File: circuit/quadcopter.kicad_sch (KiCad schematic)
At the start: 119 parts, among them J1 Conn_01x01_Female, J10 Conn_01x01_Female, J13 Conn_01x01_Female, J15 Conn_01x01_Female, J16 Conn_01x01_Female, J17 Conn_01x01_Female, J18 USB_C_Receptacle_USB2.0, J19 Conn_01x08_Male, J2 Conn_01x01_Female, J21 Conn_01x01_Female, J22 Conn_01x01_Female, J23 Conn_01x01_Female, J24 Conn_01x01_Female, J25 Conn_01x01_Female, J26 Conn_01x01_Female, J28 Conn_01x01_Female, J29 Conn_01x01_Female, J3 Conn_01x01_Female, J30 Conn_01x01_Female, J31 Conn_01x01_Female, J32 Conn_01x01_Female, J33 Conn_01x01_Female, J34 Conn_01x01_Female, J37 Conn_01x01_Female, J4 Conn_01x01_Female, J40 Conn_01x01_Female, J41 Conn_01x01_Female, J42 Conn_01x01_Female, J43 Conn_01x01_Female, J44 Conn_01x01_Female, J45 Conn_01x01_Female, J46 Conn_01x01_Female, J47 Conn_01x01_Female, J48 Conn_01x01_Female, J49 Conn_01x01_Female, J5 Conn_Coaxial, J50 Conn_01x01_Female, J6 Conn_01x06_Male, J7 Conn_01x01_Female, J8 Conn_01x01_Female, J9 Conn_01x01_Female, Q1 AO3400A, SW1 SW_DIP_x01, U1 STM32G431CBU6, U2 ICM-42605, U3 DPS310, U4 3V3, U5 EUP3458 1.2A, 30V max input, 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, U6 2450FM07D0034T, U7 W25Q80DVUXIE TR (16M), U8 SX1281, U9 5v, 500mA, Y1 16M, Y2 52Mhz, 12pF

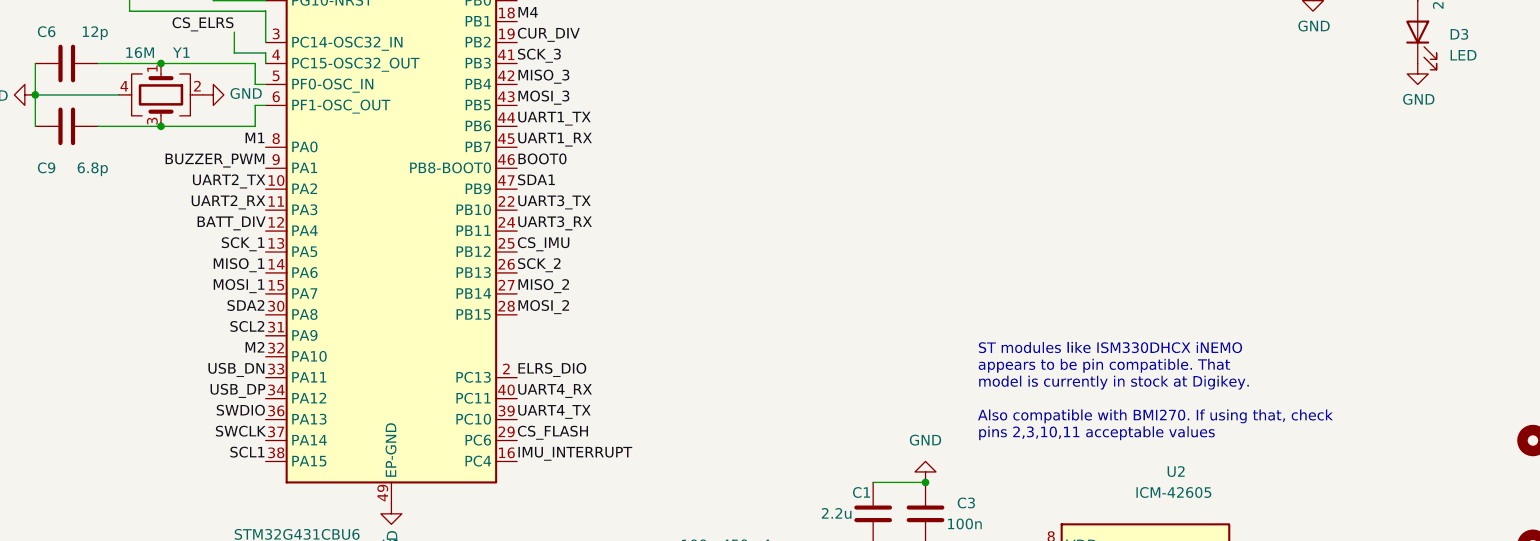
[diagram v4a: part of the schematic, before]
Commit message: A number of improvements to DSHOT/burst DMA logic
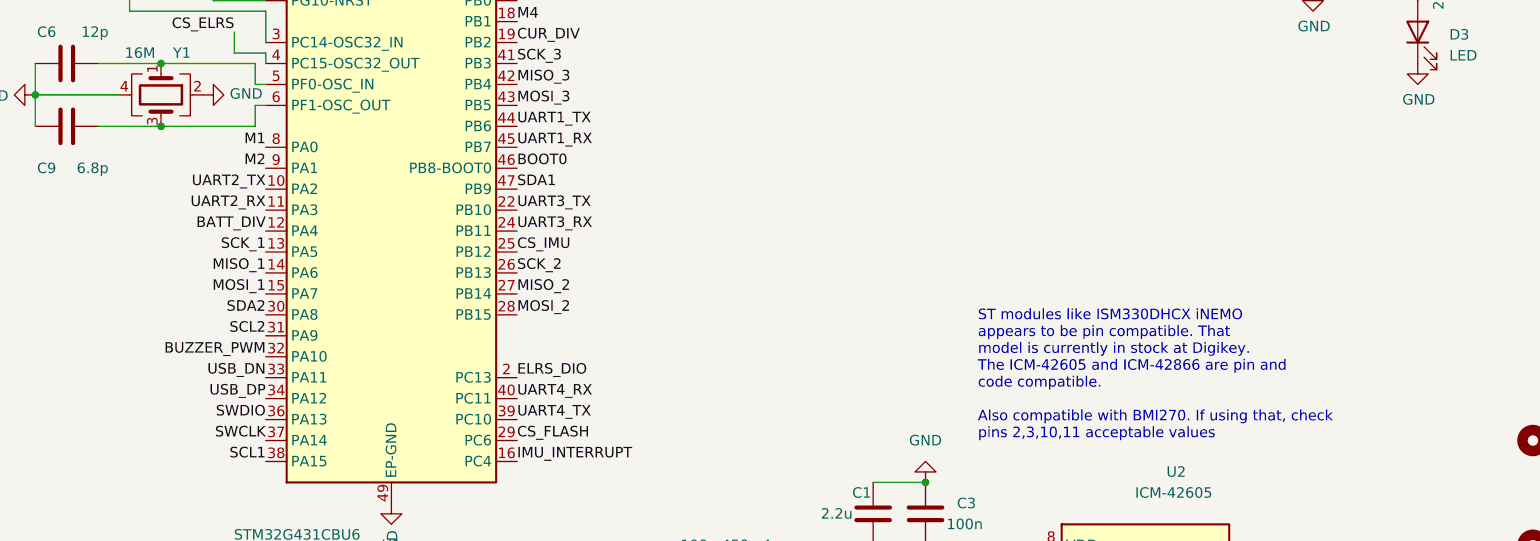
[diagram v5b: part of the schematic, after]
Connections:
- net BUZZER_PWM: now also U1.32 (PA10); no longer U1.9 (PA1)
- net M2: now also U1.9 (PA1); no longer U1.32 (PA10)
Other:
- note added: "ST modules like ISM330DHCX iNEMO appears to be pin compatible. That model is currently in stock at Digikey. The ICM-42605 and ICM-42866 are pin and code compatible. Also compatible with BMI270. If using that, check pins 2,3,10,11 acceptable values"
- note removed: "ST modules like ISM330DHCX iNEMO appears to be pin compatible. That model is currently in stock at Digikey. Also compatible with BMI270. If using that, check pins 2,3,10,11 acceptable values"
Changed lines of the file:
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@@
     (effects (font (size 1.27 1.27)) (justify left bottom))
   )
-  (text "ST modules like ISM330DHCX iNEMO\nappears to be pin compatible. That\nmodel is currently in stock at Digikey.\n\nAlso compatible with BMI270. If using that, check\npins 2,3,10,11 acceptable values\n"
+  (text "ST modules like ISM330DHCX iNEMO\nappears to be pin compatible. That\nmodel is currently in stock at Digikey.\nThe ICM-42605 and ICM-42866 are pin and\ncode compatible.\n\nAlso compatible with BMI270. If using that, check\npins 2,3,10,11 acceptable values\n"
     (at 199.39 114.3 0)
     (effects (font (size 1.27 1.27)) (justify left bottom))
@@
     (effects (font (size 1.27 1.27)) (justify left bottom))
   )
-  (label "M2" (at 113.03 104.14 180)
+  (label "M2" (at 113.03 81.28 180)
     (effects (font (size 1.27 1.27)) (justify right bottom))
   )
@@
     (effects (font (size 1.27 1.27)) (justify left bottom))
   )
-  (label "BUZZER_PWM" (at 113.03 81.28 180)
+  (label "BUZZER_PWM" (at 113.03 104.14 180)
     (effects (font (size 1.27 1.27)) (justify right bottom))
   )

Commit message: More work getting it towards a compilable state
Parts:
- J19: LCSC (none) -> C160407
- J6: LCSC (none) -> C160405; now left out of the parts list
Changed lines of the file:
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@@
+      (effects (font (size 1.27 1.27)) hide)
+    )
+    (property "LCSC" "C160407" (id 4) (at 478.79 53.34 0)
       (effects (font (size 1.27 1.27)) hide)
     )
@@
   )
   (symbol (lib_id "Connector:Conn_01x06_Male") (at 496.57 107.95 180) (unit 1)
-    (in_bom yes) (on_board yes)
+    (in_bom no) (on_board yes)
     (property "Reference" "J6" (id 0) (at 490.22 92.71 0)
       (effects (font (size 1.27 1.27)) (justify right))
@@
       (effects (font (size 1.27 1.27)) hide)
     )
+    (property "LCSC" "C160405" (id 4) (at 496.57 107.95 0)
+      (effects (font (size 1.27 1.27)) hide)
+    )

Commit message: Work on PIDs
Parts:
- U1: value STM32G431CBU6 -> STM32G474CEU6
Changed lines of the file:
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@@
     (in_bom yes) (on_board yes)
     (property "Reference" "U1" (id 0) (at 128.27 127 0))
-    (property "Value" "STM32G431CBU6" (id 1) (at 116.84 125.73 0))
+    (property "Value" "STM32G474CEU6" (id 1) (at 116.84 125.73 0))
     (property "Footprint" "Package_DFN_QFN:QFN-48-1EP_7x7mm_P0.5mm_EP5.6x5.6mm" (id 2) (at 115.57 119.38 0)
       (effects (font (size 1.27 1.27)) (justify right) hide)
@@
     )
     (path "/0340b3a8-59fc-4ac7-90dd-935a6d19ff49"
-      (reference "U1") (unit 1) (value "STM32G431CBU6") (footprint "Package_DFN_QFN:QFN-48-1EP_7x7mm_P0.5mm_EP5.6x5.6mm")
+      (reference "U1") (unit 1) (value "STM32G474CEU6") (footprint "Package_DFN_QFN:QFN-48-1EP_7x7mm_P0.5mm_EP5.6x5.6mm")
     )
     (path "/2606c3c7-aa7a-4631-9635-e40074c6e1f1"

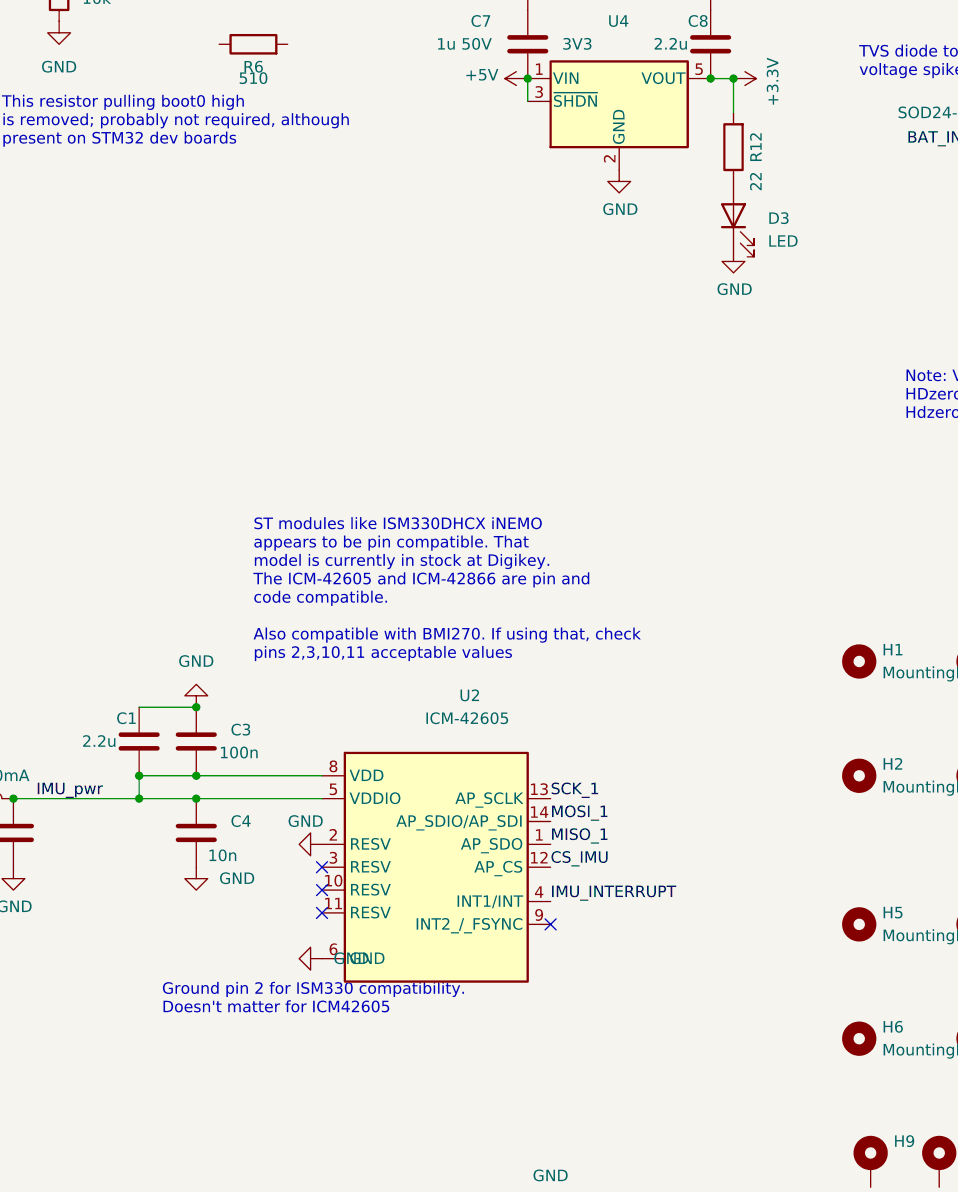
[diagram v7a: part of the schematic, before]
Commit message: More work on DSHOT, and fixes from testing on hardware
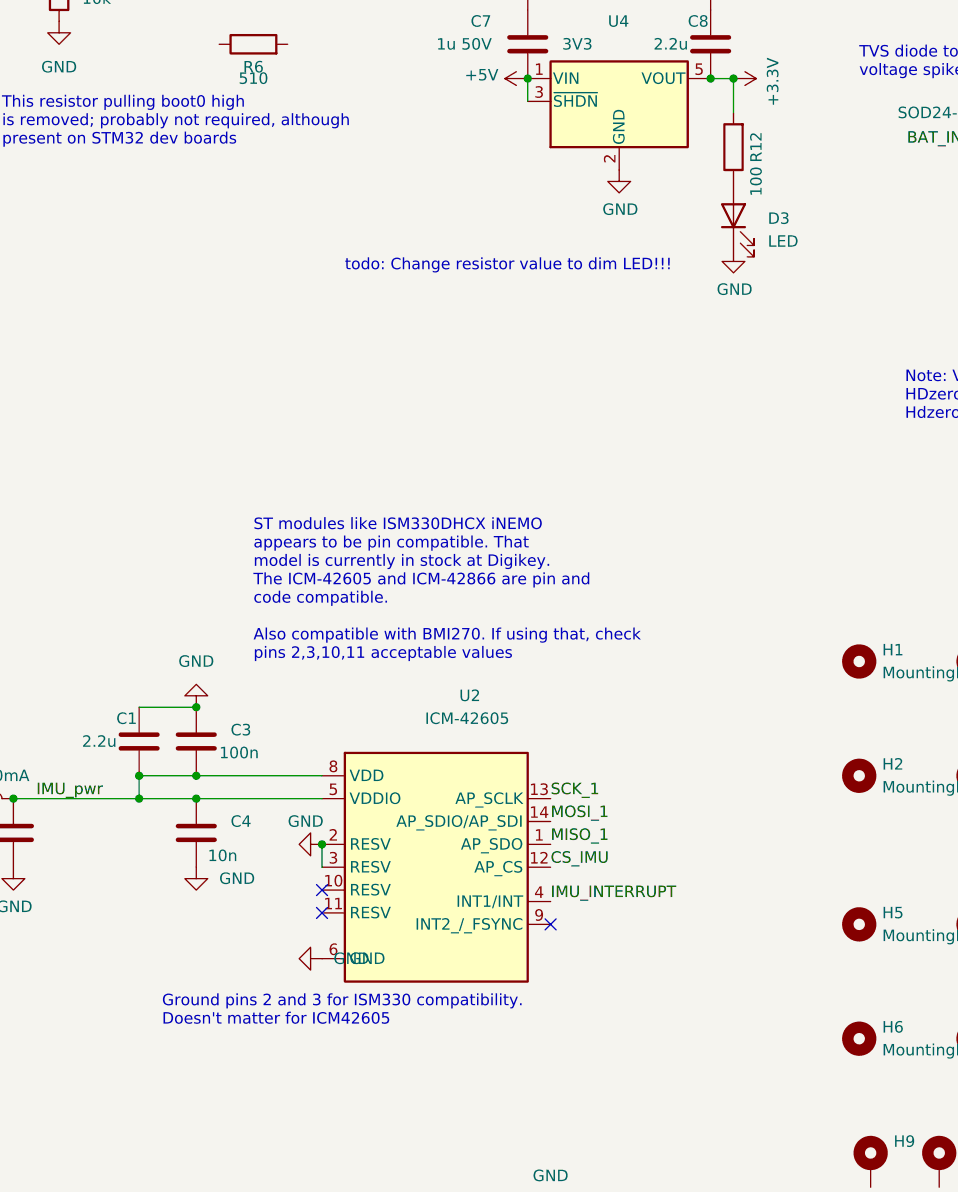
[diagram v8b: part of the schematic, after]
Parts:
- R12: value 22 -> 100; LCSC C25092 -> C25076
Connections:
- net GND: now also U2.3 (RESV)
- no-connect marks 9 -> 8
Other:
- note added: "Ground pins 2 and 3 for ISM330 compatibility. Doesn't matter for ICM42605"
- note added: "todo: Change resistor value to dim LED!!!"
- note removed: "Ground pin 2 for ISM330 compatibility. Doesn't matter for ICM42605"
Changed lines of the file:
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@@
   (junction (at 64.77 325.12) (diameter 0) (color 0 0 0 0)
   )
+  (junction (at 207.01 134.62) (diameter 0) (color 0 0 0 0)
+  )
   (junction (at 124.46 48.26) (diameter 0) (color 0 0 0 0)
   )
@@
   (no_connect (at 48.26 306.07))
   (no_connect (at 27.94 231.14))
-  (no_connect (at 207.01 137.16))
   (no_connect (at 207.01 139.7))
   (no_connect (at 207.01 142.24))
@@
     (stroke (width 0) (type default) (color 0 0 0 0))
   )
+  (wire (pts (xy 207.01 134.62) (xy 207.01 137.16))
+    (stroke (width 0) (type default) (color 0 0 0 0))
+  )
   (wire (pts (xy 289.56 -20.32) (xy 297.18 -20.32))
     (stroke (width 0) (type default) (color 0 0 0 0))
@@
     (effects (font (size 1.27 1.27)) (justify left bottom))
   )
-  (text "Ground pin 2 for ISM330 compatibility.\nDoesn't matter for ICM42605\n"
-    (at 189.23 153.67 0)
+  (text "todo: Change resistor value to dim LED!!!" (at 209.55 71.12 0)
+    (effects (font (size 1.27 1.27)) (justify left bottom))
+  )
+  (text "Ground pins 2 and 3 for ISM330 compatibility.\nDoesn't matter for ICM42605\n"
+    (at 189.23 154.94 0)
     (effects (font (size 1.27 1.27)) (justify left bottom))
   )
@@
     (in_bom yes) (on_board yes)
     (property "Reference" "R12" (id 0) (at 255.27 57.15 90))
-    (property "Value" "22" (id 1) (at 255.27 60.96 90))
+    (property "Value" "100" (id 1) (at 255.27 60.96 90))
     (property "Footprint" "Resistor_SMD:R_0402_1005Metric" (id 2) (at 254.508 57.15 90)
       (effects (font (size 1.27 1.27)) hide)
@@
       (effects (font (size 1.27 1.27)) hide)
     )
-    (property "LCSC" "C25092" (id 4) (at 252.73 57.15 0)
+    (property "LCSC" "C25076" (id 4) (at 252.73 57.15 0)
       (effects (font (size 1.27 1.27)) hide)
     )
@@
     )
     (path "/b11c4015-625f-4f88-96c9-7525d3686b6a"
-      (reference "R12") (unit 1) (value "22") (footprint "Resistor_SMD:R_0402_1005Metric")
+      (reference "R12") (unit 1) (value "100") (footprint "Resistor_SMD:R_0402_1005Metric")
     )
     (path "/427ea469-a00c-48a4-8283-a7d9e027923d"
